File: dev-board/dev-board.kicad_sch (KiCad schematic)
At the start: 43 parts, among them J1 Prog_conn, J2 Tag connect TC2030-CTX, SW1 Reset Switch, U1 nRF52840-QIAA-R/nRF52833-QIAA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, Y1 32.768kHz, Y2 32MHz

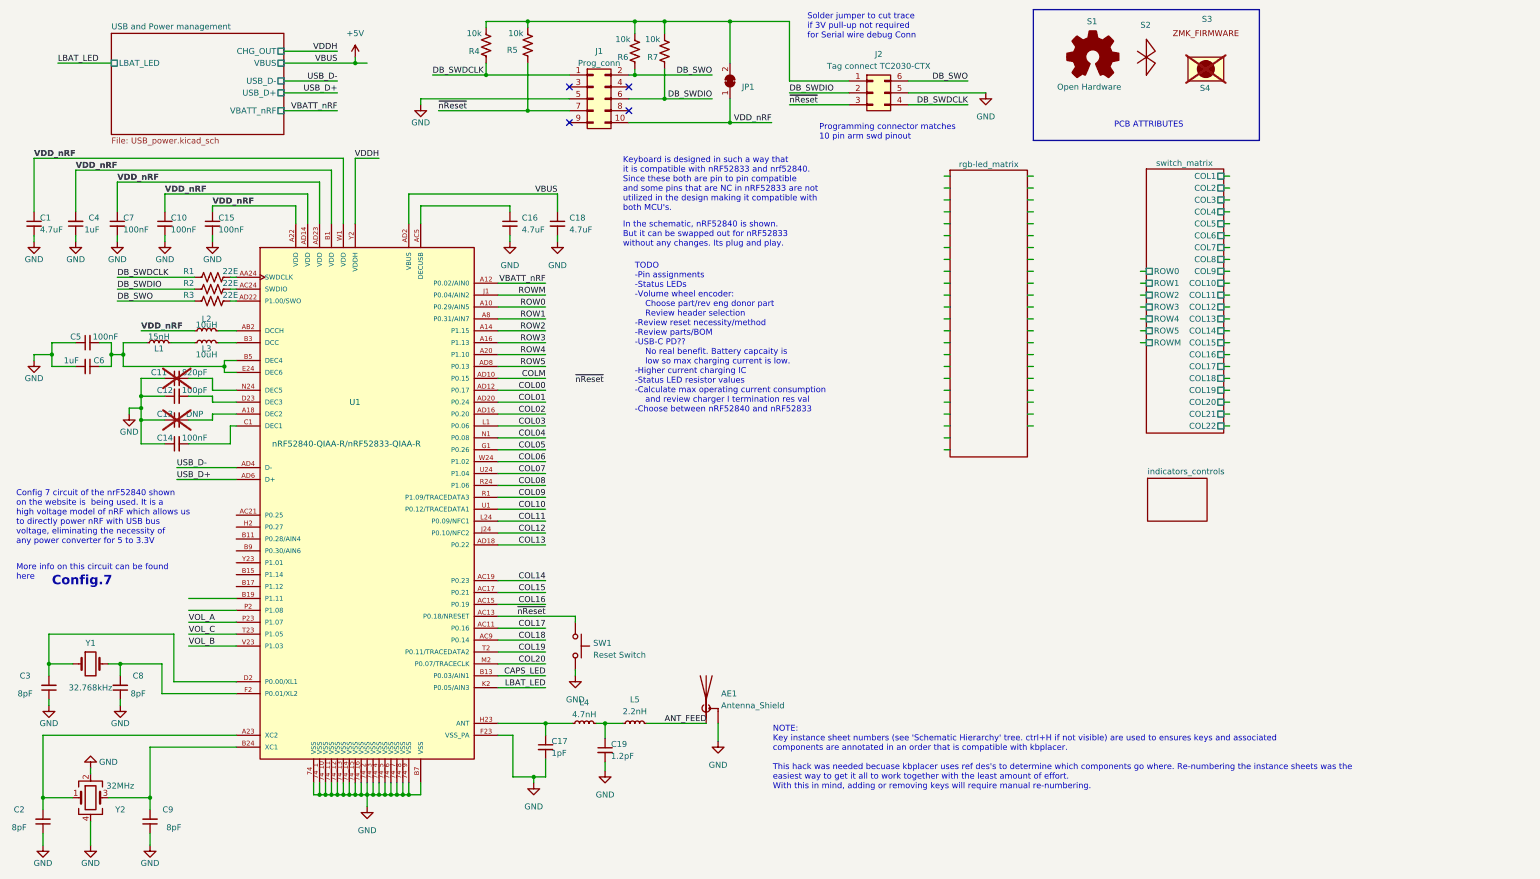
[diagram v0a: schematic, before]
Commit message: created dev-board to prove design before full-size
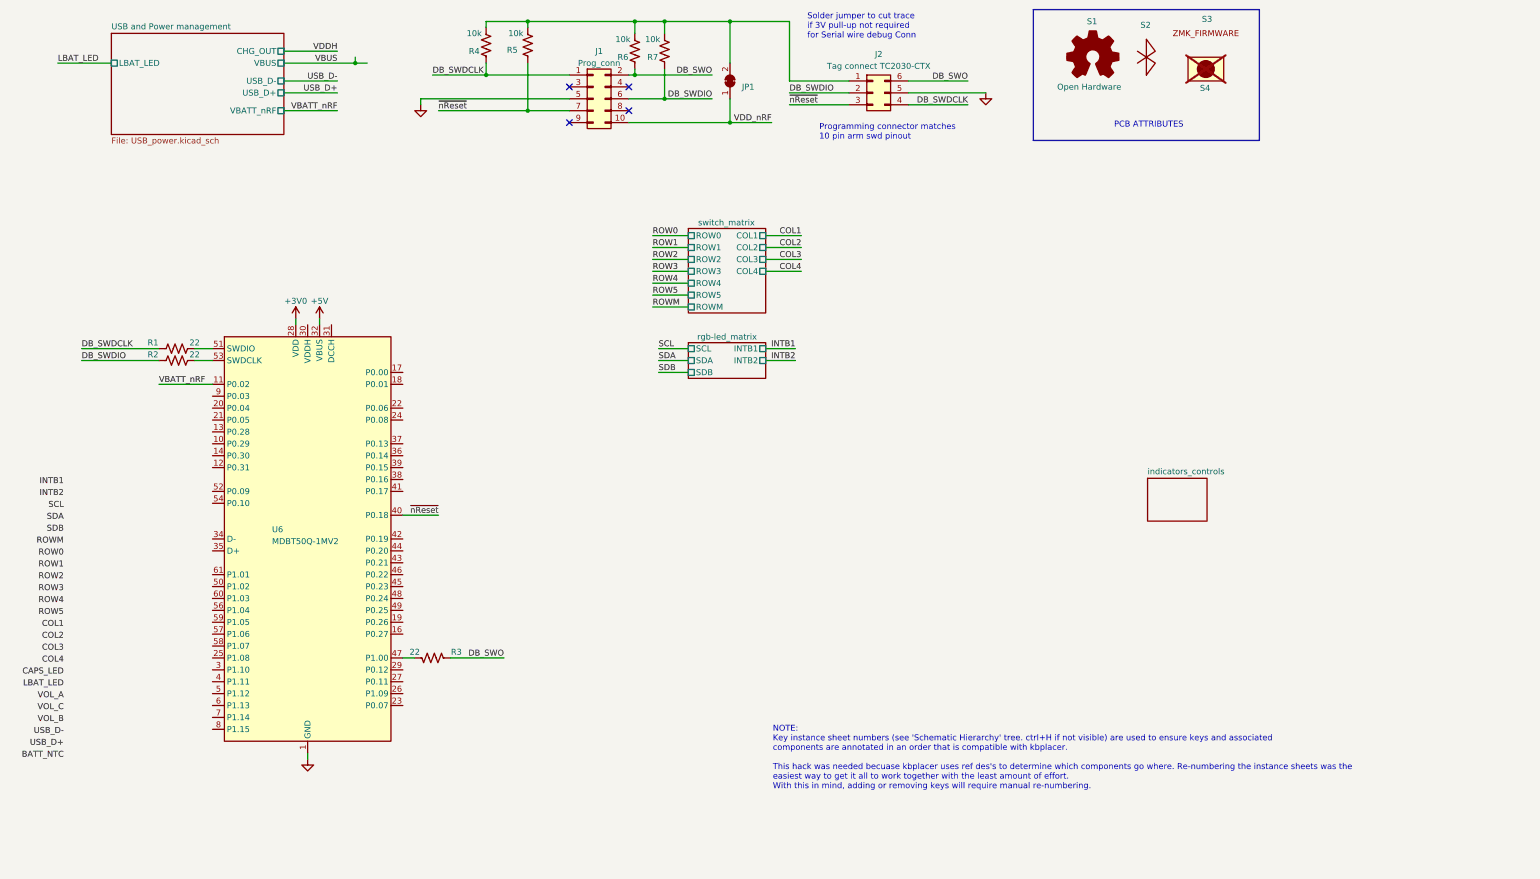
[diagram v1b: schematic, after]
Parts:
- removed AE1: Antenna_Shield, keyboard:BLE_ANTENNA, symbol keyboard:Antenna_Shield
- removed C1, C16, C18: 4.7uF, keyboard:C_0805_2012Metric, symbol keyboard:C_Small
- removed C10, C14, C15, C5, C7: 100nF, keyboard:C_0402_1005Metric, symbol keyboard:C_Small
- removed C11: 820pF, keyboard:C_0402_1005Metric, symbol keyboard:C_Small
- removed C12: 100pF, keyboard:C_0402_1005Metric, symbol keyboard:C_Small
- removed C13: DNP, keyboard:C_0402_1005Metric, symbol keyboard:C_Small
- removed C17: 1pF, keyboard:C_0402_1005Metric, symbol keyboard:C_Small
- removed C19: 1.2pF, keyboard:C_0402_1005Metric, symbol keyboard:C_Small
- removed C2, C3, C8, C9: 8pF, keyboard:C_0402_1005Metric, symbol keyboard:C_Small
- removed C4, C6: 1uF, keyboard:C_0603_1608Metric, symbol Device:C_Small
- removed L1: 15nH, keyboard:L_0402_1005Metric, symbol keyboard:L_Small
- removed L2, L3: 10uH, keyboard:L_0603_1608Metric, symbol keyboard:L_Small
- removed L4: 4.7nH, keyboard:L_0402_1005Metric, symbol keyboard:L_Small
- removed L5: 2.2nH, keyboard:L_0402_1005Metric, symbol keyboard:L_Small
- removed SW1: Reset Switch, keyboard:RST_SW, symbol keyboard:SW_Push
- removed U1: nRF52840-QIAA-R/nRF52833-QIAA-R, keyboard:aqfn73, symbol keyboard:NRF52840-QIAA-R
- removed Y1: 32.768kHz, keyboard:SMD-2_crystal, symbol keyboard:Crystal
- removed Y2: 32MHz, keyboard:SMD-4_crystal, symbol keyboard:Crystal_GND24
- added U6: MDBT50Q-1MV2, RF_Module:Raytac_MDBT50Q, symbol RF_Module:MDBT50Q-1MV2
- R1, R2, R3: value 22E -> 22
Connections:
- net +5V: now also U6.32 (VBUS)
- net GND: now also U6.1 (GND), U6.15 (GND), U6.2 (GND), U6.33 (GND), U6.55 (GND)
- net VBATT_nRF: now also U6.11 (P0.02)
- net ~{nReset}: now also U6.40 (P0.18)
- net at R1.2: now also U6.51 (SWDIO)
- net at R2.2: now also U6.53 (SWDCLK)
- net at R3.2: now also U6.47 (P1.00)
- new net +3V0: U6.28 (VDD)
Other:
- sheet rgb-led_matrix ports: added INTB1, INTB2, SCL, SDA, SDB; removed none
- sheet switch_matrix ports: added none; removed COL10, COL11, COL12, COL13, COL14, COL15, COL16, COL17, COL18, COL19, COL20, COL21, COL22, COL5, COL6, COL7, COL8, COL9
- note added: "NOTE: Key instance sheet numbers (see 'Schematic Hierarchy' tree. ctrl+H if not visible) are used to ensure keys and associated components are annotated in an order that is compatible with kbplacer. This hack was needed becuase kbplacer uses ref des's to determine which components go where. Re-numbering the instance sheets was the easiest way to get it all to work together with the least amount o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"
- note removed: "Config 7 circuit of the nrF52840 shown on the website is being used. It is a high voltage model of nRF which allows us to directly power nRF with USB bus voltage, eliminating the necessity of any power converter for 5 to 3.3V"
- note removed: "Config.7"
- note removed: "In the schematic, nRF52840 is shown. But it can be swapped out for nRF52833 without any changes. Its plug and play."
- note removed: "Keyboard is designed in such a way that it is compatible with nRF52833 and nrf52840. Since these both are pin to pin compatible and some pins that are NC in nRF52833 are not utilized in the design making it compatible with both MCU's."
- note removed: "More info on this circuit can be found here"
- note removed: "NOTE: Key instance sheet numbers (see 'Schematic Hierarchy' tree. ctrl+H if not visible) are used to ensures keys and associated components are annotated in an order that is compatible with kbplacer. This hack was needed becuase kbplacer uses ref des's to determine which components go where. Re-numbering the instance sheets was the easiest way to get it all to work together with the least amount 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"
- note removed: "TODO -Pin assignments -Status LEDs -Volume wheel encoder: Choose part/rev eng donor part Review header selection -Review reset necessity/method -Review parts/BOM -USB-C PD?? No real benefit. Battery capcaity is low so max charging current is low. -Higher current charging IC -Status LED resistor values -Calculate max operating current consumption and review charger I termination res val -Choose be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"
- moved on the sheet: R2

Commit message: battery charger components
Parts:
- added R29, R30: 22, keyboard:R_0402_1005Metric, symbol keyboard:R_US
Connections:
- net +5V is gone; now on net VBUS: U6.32 (VBUS)
- net +3V0: now also U6.30 (VDDH)
- net DB_SWDCLK: now also U6.42 (P0.19)
- net DB_SWDIO: now also U6.44 (P0.20)
- net USB_D+: now also R30.1
- net USB_D-: now also R29.1
- net at JP1.2 (B), R4.2, R5.2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: no longer J2.1 (Pin_1)
- net at U6.34 (D-): now also R29.2
- net at U6.35 (D+): now also R30.2
- net VDD_nRF renamed VSYS
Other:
- sheet USB and Power management ports: added none; removed LBAT_LED
- moved on the sheet: JP1
